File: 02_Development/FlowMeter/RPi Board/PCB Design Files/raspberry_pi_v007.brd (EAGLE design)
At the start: 111.8 x 128.3 mm, 136 parts, among them J3 277-2419-ND, J5 POWER_JACK, J7 277-2419-ND, J8 277-2419-ND, J9 277-2419-ND, P1 SPL006-007, P2 SPL006-007, P3 SPL006-007, P4 SPL006-007, P5 SPL006-007, Q1 4.3A/20V/54mΩ, Q2 500mA/300V, U1 P82B715TD, U5 P82B715TD, U6 TCA9548APWR, U7 TCA9548APWR, U8 P82B715TD, U9 P82B715TD

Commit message: Raspberry Pi PSV v007
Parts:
- removed ADC1: ADC128_8CH, th_libraries:TSSOP16
- added U2: TCA9548APWR, microbuilder:TSSOP24
- C10, C12: value 100nF -> 33n
- C11: value 100n -> 33n
- C14: value 1uF -> 470n
- C15: value 1uF -> 4.7pF; device SparkFun-Capacitors:0805 -> SparkFun-Capacitors:0603
- C16: value 33n -> 470nF
- C17: value 33n -> 100n
- C18: value 470n -> 10uF; device SparkFun-Capacitors:0805 -> microbuilder:0805-NO
- C2, C26, C30, C6: value 100nF -> 100n
- C21: value 330uF -> 100nF; device SparkFun-Capacitors:PANASONIC_G -> SparkFun-Capacitors:0805
- C22: value 22uF -> 100nF; device microbuilder:_1206 -> SparkFun-Capacitors:0805
- C23, C24: value 100nF -> 22uF; device SparkFun-Capacitors:0805 -> microbuilder:_1206
- C25: value 22uF -> 330uF; device microbuilder:_1206 -> SparkFun-Capacitors:PANASONIC_G
- C27: value 10uF -> 10u
- C28: value 470nF -> 100n
- C29: value 4.7pF -> 100nF; device SparkFun-Capacitors:0603 -> SparkFun-Capacitors:0805
- C3: value 100nF -> 1uF
- C4: value 33n -> 100nF
- C5: value 33n -> 1uF
- C7: value 10uF -> 100nF; device microbuilder:0805-NO -> SparkFun-Capacitors:0805
- C8: value 10u -> 33n; device microbuilder:0805-NO -> SparkFun-Capacitors:0805
- C9: value 100n -> 10uF; device SparkFun-Capacitors:0805 -> microbuilder:0805-NO
- J1, J2, J4: value (none) -> NP (277-2415-ND)
- J10: value (none) -> 277-2419-ND; device SparkFun-Connectors:1X02 -> th_libraries:1X04_3.5MM_RA
- J11: value (none) -> POWER_JACK; device SparkFun-Connectors:SCREWTERMINAL-5MM-2 -> SparkFun-Connectors:POWER_JACK_PTH
- J3: value 277-2419-ND -> NP (277-2415-ND); device th_libraries:1X04_3.5MM_RA -> SparkFun-Connectors:SCREWTERMINAL-3.5MM-3
- J5: value POWER_JACK -> 277-2419-ND; device SparkFun-Connectors:POWER_JACK_PTH -> th_libraries:1X04_3.5MM_RA
- J6: value (none) -> 277-2419-ND; device SparkFun-Connectors:SCREWTERMINAL-3.5MM-3 -> th_libraries:1X04_3.5MM_RA
- J7: value 277-2419-ND -> 732-5315-ND; device th_libraries:1X04_3.5MM_RA -> SparkFun-Connectors:1X02
- J9: value 277-2419-ND -> 732-5315-ND; device th_libraries:1X04_3.5MM_RA -> SparkFun-Connectors:SCREWTERMINAL-5MM-2
- Q1: value 4.3A/20V/54mΩ -> 500mA/300V
- Q2: value 500mA/300V -> 4.3A/20V/54mΩ
- R1, R2: value 470 -> 100; device SparkFun-Resistors:0805 -> SparkFun-Passives:0805
- R11, R52: value 10K -> 2K; device SparkFun-Resistors:0805 -> SparkFun-Passives:0805
- R12: value 2K -> 10K; device SparkFun-Passives:0805 -> SparkFun-Resistors:0805
- R13, R16, R18, R31, R35: value 3K -> 10K
- R17, R29, R8: value 3K -> 100; device SparkFun-Resistors:0805 -> SparkFun-Passives:0805
- R20, R40, R41, R42, R6: value 10K -> 3K
- R21: value 10k -> 3K
- R23: value 1K -> 10k; device SparkFun-Passives:0805 -> SparkFun-Resistors:0805
- R24, R3: value 1K -> 100
- R25: value 10K -> 100; device SparkFun-Resistors:0805 -> SparkFun-Passives:0805
- R26: value 100 -> 10K; device SparkFun-Passives:0805 -> SparkFun-Resistors:0805
- R27: value 100 -> 49.9K
- R28: value 100 -> 365K
- R30: value 3K -> 470
- R32: value 3K -> 100K; device SparkFun-Resistors:0805 -> SparkFun-Passives:0805
- R36: value 3K -> 1K; device SparkFun-Resistors:0805 -> SparkFun-Passives:0805
- R37, R38, R4, R43: value 100 -> 3K; device SparkFun-Passives:0805 -> SparkFun-Resistors:0805
- R39: value 10K -> 470
- R44: value 100 -> 470; device SparkFun-Passives:0805 -> SparkFun-Resistors:0805
- R45: value 1K -> 470; device SparkFun-Passives:0805 -> SparkFun-Resistors:0805
- R46: value 0 -> 10K
- R48: value 10K -> 0
- R49: value 365K -> 470; device SparkFun-Passives:0805 -> SparkFun-Resistors:0805
- R5: value 2K -> 3K; device SparkFun-Passives:0805 -> SparkFun-Resistors:0805
- R50: value 49.9K -> 10K; device SparkFun-Passives:0805 -> SparkFun-Resistors:0805
- R51: value 100K -> 10K; device SparkFun-Passives:0805 -> SparkFun-Resistors:0805
- R53, R55, R56: value 470 -> 1K; device SparkFun-Resistors:0805 -> SparkFun-Passives:0805
- U1: value P82B715TD -> ADC128_8CH; device Volks73-NXPSemiconductors:SOIC-8 -> th_libraries:TSSOP16
- U6: value TCA9548APWR -> P82B715TD; device microbuilder:TSSOP24 -> Volks73-NXPSemiconductors:SOIC-8
- moved C10 97.6 mm to (-11.4, 21.5), turned to 90 degrees
- moved J5 86.4 mm to (-26.7, -2.54), turned to 270 degrees
- moved C13 86.1 mm to (64.8, 11.2)
- moved C2 84.8 mm to (-12.8, 45.5)
- moved R1 84.8 mm to (-16.4, 50.0), turned to 270 degrees
- moved J3 81.3 mm to (-26.7, 25.4)
- moved C12 81.1 mm to (-11.4, 13.2), turned to 90 degrees
- moved C4 78.6 mm to (64.8, 36.6), turned to 0 degrees
- moved C3 77.8 mm to (-12.8, 42.4)
- moved P1 76.2 mm to (64.8, 39.2)
- moved R3 76.2 mm to (-15.7, 21.6), turned to 90 degrees
- moved J6 73.7 mm to (-26.7, -20.3)
- moved U6 72.7 mm to (-20.8, -29.6)
- moved P5 71.2 mm to (64.8, -37.0), turned to 90 degrees
- moved U1 67.2 mm to (-15.1, 37.3), turned to 180 degrees
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- renumbered D5 to D3, INDUCT to L1, REF1 to U3, RPI2 to RPI3B+, TPS to U4, U$15 to HOLE7, U$20 to TP4, U$23 to HOLE10, U$26 to HOLE1, U$31 to TP3, U$35 to HOLE9, U$36 to HOLE2, U$40 to TP1, U$45 to HOLE8, U$58 to HOLE3, U$59 to TP2, U$60 to HOLE4, U$61 to HOLE5, U$62 to HOLE6, U$64 to TP5
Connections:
- removed net N$10: Q2.1, R24.1, R48.2
- removed net N$11: C29.2, R49.1, R50.1, U4.2
- removed net N$12: ADC1.8, C1.1, R4.2
- removed net N$13: R11.2, R4.1, R5.1
- removed net N$14: C24.1, U4.7
- removed net N$15: D4.C, R23.2
- removed net N$16: D3.C, R45.2
- removed net N$17: R51.1, U4.4
- removed net N$18: ADC1.4, C4.1, R26.1
- removed net N$19: ADC1.6, C5.1, R27.1
- removed net N$2: D2.C, R12.2
- removed net N$20: ADC1.5, C16.1, R28.1
- removed net N$22: ADC1.7, C17.1, R37.1
- removed net N$23: ADC1.16, R38.2
- removed net N$24: ADC1.15, R43.2
- removed net N$25: ADC1.14, R44.2
- removed net N$27: R52.2, U4.1
- removed net N$6: C24.2, L1.1, U4.6
- removed net N$7: C28.1, R51.2, U4.3
- removed net N$8: D1.C, R3.2
- removed net N$9: Q1.1, Q2.3, R47.1
- new net 12V-LED-R: D1.C, R52.2
- new net 3.3V-LED-R: D3.C, R55.2
- new net 5V-LED-R: D2.C, R53.2
- new net 5VREG-EN: R26.2, U4.1
- new net 5VREG-PG: R32.1, U4.4
- new net 5VREG-SW: C21.2, L1.1, U4.6
- new net 5VREG-VBST: C21.1, U4.7
- new net 5VREG-VFB: C15.2, R27.1, R28.1, U4.2
- new net 5VREG-VREG: C16.1, R32.2, U4.3
- new net ADC-12V-SENSE: R11.1, R16.2, R17.1
- new net ADC-DIN: R29.2, U1.14
- new net ADC-DOUT: R25.2, U1.15
- new net ADC-IN0: C11.1, R8.1, U1.4
- new net ADC-IN1: C10.1, R3.1, U1.5
- new net ADC-IN2: C8.1, R2.1, U1.6
- new net ADC-IN3: C1.1, R1.1, U1.7
- new net ADC-IN4: C12.1, R17.2, U1.8
- new net ADC-SCLK: R24.2, U1.16
- new net PI5V-LED-R: D4.C, R56.2
- new net SENS_POWER_BASE: Q1.1, R35.2, R36.1
- new net SENS_POWER_GATE: Q1.3, Q2.1, R31.1
- net 00LX: now also J6.3, R44.1, U6.7; no longer J7.3, R2.1, U1.7
- net 00LY: now also J6.4, R45.1, U6.2; no longer J7.4, R1.1, U1.2
- net 00SCL: now also R38.1, U6.3; no longer R30.1, U1.3
- net 00SDA: now also R37.1, U6.6; no longer R29.1, U1.6
- net 0SCL: now also P5.4, R20.1, U2.5; no longer P1.4, R8.1, U6.5
- net 0SDA: now also P5.3, R21.1, U2.4; no longer P1.3, R7.1, U6.4
- net 11LX: now also J10.3, R57.1, U9.7; no longer J3.3, R56.1, U8.7
- net 11LY: now also J10.4, R58.1, U9.2; no longer J3.4, R55.1, U8.2
- net 11SCL: now also R43.1, U9.3; no longer R32.1, U8.3
- net 11SDA: now also R42.1, U9.6; no longer R31.1, U8.6
- net 12V: now also C18.1, C22.1, C25.+, D1.A, J11.PWR, J3.1, R16.1, R26.1; no longer C20.1, C21.+, C27.1, D2.A, J5.PWR, J6.1, R11.1, R52.1
- net 1SCL: now also P4.4, R14.1, U2.7; no longer P2.4, R10.1, U6.7
- net 1SDA: now also P4.3, R15.1, U2.6; no longer P2.3, R9.1, U6.6
- net 22LX: now also R49.1, U8.7; no longer R58.1, U9.7
- net 22LY: now also R54.1, U8.2; no longer R57.1, U9.2
- net 22SCL: now also R40.1, U8.3; no longer R34.1, U9.3
- net 22SDA: now also R41.1, U8.6; no longer R33.1, U9.6
- net 2SCL: now also R9.1, U2.9; no longer R14.1, U6.9
- net 2SDA: now also R10.1, U2.8; no longer R13.1, U6.8
- net 3.3V: now also C13.1, C20.1, C27.1, C29.1, C4.1, C5.1, R19.1, R20.2, R23.2, R35.1, R4.2, R46.2, R5.2, R50.1, R6.2, U1.13, U2.24; no longer ADC1.13, C10.1, C12.1, C15.1, C2.1, C3.1, C8.1, R13.2, R16.2, R17.2, R18.2, R41.2, R42.1, R48.1, R6.1, R8.2, U6.24
- net 33LX: now also J5.3, R30.1; no longer J9.3, R54.1
- net 33LY: now also J5.4, R39.1; no longer J9.4, R53.1
- net 33SCL: now also R33.1; no longer R36.1
- net 33SDA: now also R34.1; no longer R35.1
- net 3SCL: now also P1.4, R6.1, U2.11; no longer P4.4, R16.1, U6.11
- net 3SDA: now also P1.3, R7.1, U2.10; no longer P4.3, R15.1, U6.10
- net 4.096V: now also C2.1, C3.1, U1.2; no longer ADC1.2, C11.1, C14.1
- net 4SCL: now also P2.4, R4.1, U2.14; no longer P5.4, R18.1, U6.14
- net 4SDA: now also P2.3, R5.1, U2.13; no longer P5.3, R17.1, U6.13
- net 5V: now also C15.1, C23.1, C24.1, D2.A, J7.2, R28.2; no longer C22.1, C25.1, C29.1, D4.A, J10.2, R49.2
- net A0_PC: now also R13.1, U2.1; no longer R19.1, U6.1
- net A1_PC: now also R18.1, U2.2; no longer R20.1, U6.2
- net A2_PC: now also R12.1, U2.21; no longer R25.1, U6.21
- net A3_PC: now also R51.1; no longer R39.1
- net A4_PC: now also R47.1; no longer R40.1
- net A5_PC: now also R46.1; no longer R41.1
- net ADC1: now also J4.3, R8.2; no longer J1.3, R26.2
- net ADC2: now also J3.3, R3.2; no longer J2.3, R28.2
- net ADC3: now also J2.3, R2.2; no longer J4.3, R27.2
- net ADC4: now also J1.3, R1.2; no longer J6.3, R37.2
- net GND: now also C24.2, C25.-, C29.2, J10.2, J11.GND, J11.GNDBREAK, J5.2, J9.1, Q1.2, R11.2, R12.2, R13.2, R18.2, R27.2, R47.2, R48.2, R51.2, R52.1, R53.1, R55.1, R56.1, U1.1, U1.12, U1.3, U2.12, U6.4; no longer ADC1.1, ADC1.12, ADC1.3, C15.2, C21.-, C25.2, J11.1, J5.GND, J5.GNDBREAK, J7.2, J9.2, Q2.2, R12.1, R19.2, R20.2, R23.1, R25.2, R3.1, R39.2, R40.2, R45.1, R46.2, R5.2, R50.2, U1.4, U6.12
- net GND1: now also R48.1; no longer R46.1
- net GPIO12: now also R36.2; no longer R24.2
- net PI_5V_POWER: now also C14.1, D4.A, J7.1, J9.2, Q2.2, R31.2; no longer C18.1, D1.A, J10.1, J11.2, Q1.2, R47.2
- net RESET: now also R19.2, R50.2, U2.3; no longer R42.2, R6.2, U6.3
- net SCL: now also U2.22; no longer U6.22
- net SDA: now also R23.1, U2.23; no longer R21.1, U6.23
- net SENS_POWER: now also C17.1, C28.1, J10.1, J5.1, J6.1, Q2.3, R37.2, R38.2, R39.2, R40.2, R41.2, R42.2, R43.2, R44.2, R45.2, R49.2, U6.8; no longer C13.1, C23.1, J3.1, J7.1, J9.1, Q1.3, R1.2, R2.2, R29.2, R31.2, R32.2, R35.2, R36.2, R53.2, R55.2, R56.2, U1.8
- net SPI_MISO: now also R25.1; no longer R43.1
- net SPI_MOSI: now also R29.1; no longer R44.1
- net SPI_SCLK: now also R24.1; no longer R38.1
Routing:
- net GND: track 72.9 -> 201.3 mm, vias 9 -> 15
- net N$12: track 70.3 -> 0.00 mm
- net ADC-IN4: track 0.00 -> 70.3 mm
- net N$25: track 45.0 -> 0.00 mm, vias 2 -> 0
- net ADC-DIN: track 0.00 -> 45.0 mm, vias 0 -> 2
- net N$24: track 40.5 -> 0.00 mm, vias 2 -> 0
- net ADC-DOUT: track 0.00 -> 40.5 mm, vias 0 -> 2
- net N$23: track 34.5 -> 0.00 mm, vias 2 -> 0
- net ADC-SCLK: track 0.00 -> 34.4 mm, vias 0 -> 2
- net N$18: track 29.5 -> 0.00 mm
- net ADC-IN0: track 0.00 -> 29.5 mm
- net N$20: track 25.1 -> 0.00 mm, vias 2 -> 0
- net ADC-IN1: track 0.00 -> 25.1 mm, vias 0 -> 2
- net N$19: track 23.2 -> 0.00 mm
- net ADC-IN2: track 0.00 -> 23.2 mm
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- added copper zone on layer 1, net 5VREG-SW
- removed copper zone on layer 1, net N$6
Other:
- board text added: "Airflow and Pressure Sensor PI Hat Project Tetra Thomas Hudson et al. 01/01/2021 v0.00.007"
- board text removed: "Airflow and Pressure Sensor PI Hat Project Tetra Thomas Hudson 31/12/2020 v0.00.006"

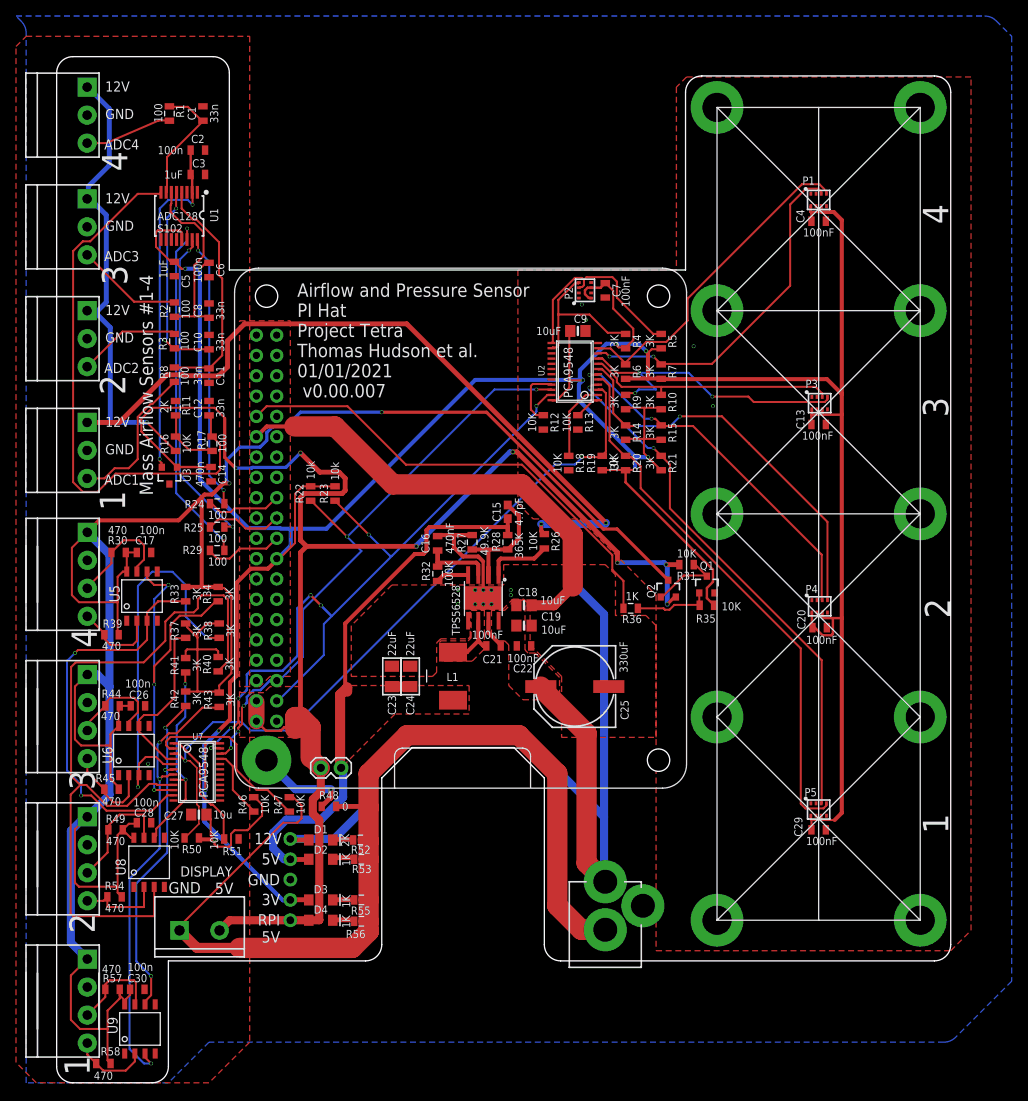
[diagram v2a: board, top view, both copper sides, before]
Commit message: add fiducials & CAD step file, cleanup
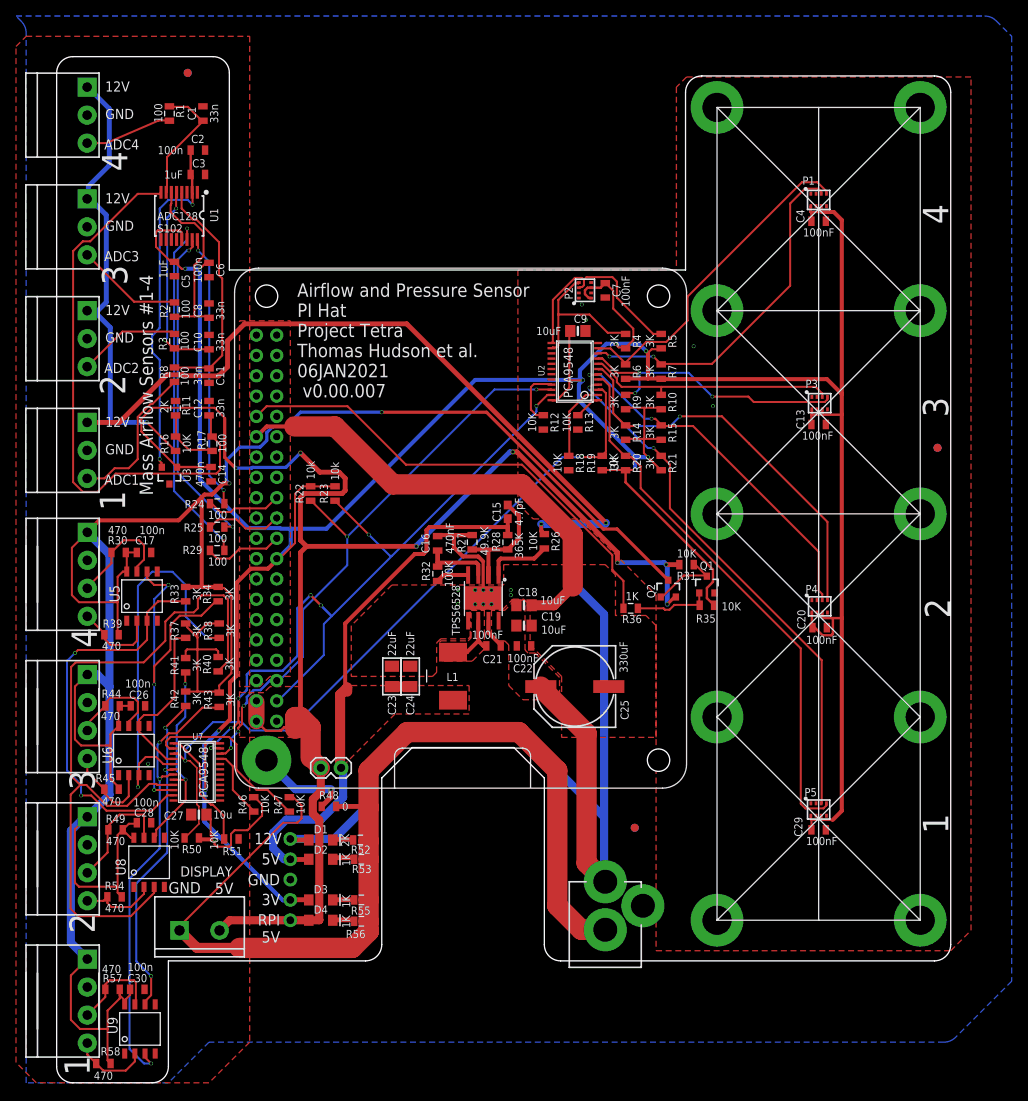
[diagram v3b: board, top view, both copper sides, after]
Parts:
- added FD1, FD2, FD3: FID_40MIL, Fiducial:FID_040
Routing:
- net 2SCL: track 38.5 -> 35.5 mm
- net 22SCL: track 95.1 -> 93.0 mm
- net SCL: track 76.3 -> 74.8 mm
- net 22LY: track 11.1 -> 9.81 mm
- net 4.096V: track 44.2 -> 44.9 mm
- net GND: track 201.3 -> 201.8 mm
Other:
- outline, holes or cut-outs redrawn
- board text added: "Airflow and Pressure Sensor PI Hat Project Tetra Thomas Hudson et al. 06JAN2021 v0.00.007"
- board text removed: "Airflow and Pressure Sensor PI Hat Project Tetra Thomas Hudson et al. 01/01/2021 v0.00.007"
